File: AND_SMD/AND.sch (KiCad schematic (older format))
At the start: 8 parts, among them J1 Conn_01x08_Male, J2 Conn_01x08_Male, J3 Conn_01x08_Male, J4 Conn_01x04_Male, U1 74LS573, U2 74LS08, U3 74LS08

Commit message: Polishing AND SMD cmd
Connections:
- net at J1.8 (Pin_8): now also U2.2; no longer U2.1
- net at J2.8 (Pin_8): now also U2.1; no longer U2.2
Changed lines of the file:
@@
 U 1 1 5F5151F7
 P 3550 4400
-F 0 "U2" H 3500 4600 50  0000 C CNN
-F 1 "74LS08" H 3750 4600 50  0000 C CNN
+F 0 "U2" H 3475 4200 50  0000 C CNN
+F 1 "74LS08" H 3750 4200 50  0000 C CNN
 F 2 "Package_SO:SO-14_3.9x8.65mm_P1.27mm" H 3550 4400 50  0001 C CNN
 F 3 "http://www.ti.com/lit/gpn/sn74LS08" H 3550 4400 50  0001 C CNN
 	1    3550 4400
-	1    0    0    -1
+	1    0    0    1
 $EndComp
 $Comp

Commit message: AND SMD PCB is ready
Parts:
- added D1: LED, LED_SMD:LED_0805_2012Metric_Pad1.15x1.40mm_HandSolder, symbol Device:LED
- added R1: 1k, Resistor_SMD:R_0805_2012Metric_Pad1.20x1.40mm_HandSolder, symbol Device:R
- J1, J2, J3: footprint Connector_PinHeader_2.54mm:PinHeader_1x08_P2.54mm_Horizontal -> Connector_PinHeader_2.54mm:PinHeader_1x08_P2.54mm_Vertical
- J4: footprint Connector_PinHeader_2.54mm:PinHeader_1x04_P2.54mm_Horizontal -> Connector_PinHeader_2.54mm:PinHeader_1x04_P2.54mm_Vertical
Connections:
- net VCC: now also D1.1 (K)
- net A7: now reaches J1.1 (Pin_1), U3.9
- net A0: now reaches J1.8 (Pin_8), U2.2
- net B7: now reaches J2.1 (Pin_1), U3.10
- net B0: now reaches J2.8 (Pin_8), U2.1
- net OUT7: now reaches J3.1 (Pin_1), U1.19 (Q0)
- net OUT0: now reaches J3.8 (Pin_8), U1.12 (Q7)
- net ~OE: now reaches J4.1 (Pin_1), U1.1 (OE)
- net ~OE: now also R1.2
- net Latch: now reaches J4.4 (Pin_4), U1.11 (Load)
- new net: D1.2 (A), R1.1
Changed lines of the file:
@@
 F 0 "J1" H 1858 3581 50  0000 C CNN
 F 1 "Conn_01x08_Male" H 1858 3490 50  0000 C CNN
-F 2 "Connector_PinHeader_2.54mm:PinHeader_1x08_P2.54mm_Horizontal" H 1750 3100 50  0001 C CNN
+F 2 "Connector_PinHeader_2.54mm:PinHeader_1x08_P2.54mm_Vertical" H 1750 3100 50  0001 C CNN
 F 3 "~" H 1750 3100 50  0001 C CNN
 	1    1750 3100
@@
 F 0 "J2" H 1858 4581 50  0000 C CNN
 F 1 "Conn_01x08_Male" H 1858 4490 50  0000 C CNN
-F 2 "Connector_PinHeader_2.54mm:PinHeader_1x08_P2.54mm_Horizontal" H 1750 4100 50  0001 C CNN
+F 2 "Connector_PinHeader_2.54mm:PinHeader_1x08_P2.54mm_Vertical" H 1750 4100 50  0001 C CNN
 F 3 "~" H 1750 4100 50  0001 C CNN
 	1    1750 4100
@@
 F 0 "J3" H 7308 3831 50  0000 C CNN
 F 1 "Conn_01x08_Male" H 7300 2775 50  0000 C CNN
-F 2 "Connector_PinHeader_2.54mm:PinHeader_1x08_P2.54mm_Horizontal" H 7200 3350 50  0001 C CNN
+F 2 "Connector_PinHeader_2.54mm:PinHeader_1x08_P2.54mm_Vertical" H 7200 3350 50  0001 C CNN
 F 3 "~" H 7200 3350 50  0001 C CNN
 	1    7200 3350
@@
 F 0 "J4" H 1825 4775 50  0000 C CNN
 F 1 "Conn_01x04_Male" H 1625 5375 50  0000 C CNN
-F 2 "Connector_PinHeader_2.54mm:PinHeader_1x04_P2.54mm_Horizontal" H 1750 5150 50  0001 C CNN
+F 2 "Connector_PinHeader_2.54mm:PinHeader_1x04_P2.54mm_Vertical" H 1750 5150 50  0001 C CNN
 F 3 "~" H 1750 5150 50  0001 C CNN
 	1    1750 5150
@@
 	2025 5250 2025 5675
 Wire Wire Line
-	2025 5675 5750 5675
+	2025 5675 3725 5675
 Wire Wire Line
 	5750 5675 5750 4050
@@
 	1    0    0    -1
 $EndComp
+$Comp
+L Device:LED D1
+U 1 1 63459271
+P 3725 5225
+F 0 "D1" V 3672 5305 50  0000 L CNN
+F 1 "LED" V 3763 5305 50  0000 L CNN
+F 2 "LED_SMD:LED_0805_2012Metric_Pad1.15x1.40mm_HandSolder" H 3725 5225 50  0001 C CNN
+F 3 "~" H 3725 5225 50  0001 C CNN
+	1    3725 5225
+	0    1    1    0
+$EndComp
+$Comp
+L Device:R R1
+U 1 1 63459C8B
+P 3725 5525
+F 0 "R1" H 3795 5571 50  0000 L CNN
+F 1 "1k" V 3725 5475 50  0000 L CNN
+F 2 "Resistor_SMD:R_0805_2012Metric_Pad1.20x1.40mm_HandSolder" V 3655 5525 50  0001 C CNN
+F 3 "~" H 3725 5525 50  0001 C CNN
+	1    3725 5525
+	1    0    0    -1
+$EndComp
+Connection ~ 3725 5675
+Wire Wire Line
+	3725 5675 5750 5675
+$Comp
+L power:VCC #PWR03
+U 1 1 6345A840
+P 3725 5075
+F 0 "#PWR03" H 3725 4925 50  0001 C CNN
+F 1 "VCC" H 3742 5248 50  0000 C CNN
+F 2 "" H 3725 5075 50  0001 C CNN
+F 3 "" H 3725 5075 50  0001 C CNN
+	1    3725 5075
+	1    0    0    -1
+$EndComp
+Text Label 2000 3500 0    50   ~ 0
+A0
+Text Label 2000 2800 0    50   ~ 0
+A7
+Text Label 2025 4500 0    50   ~ 0
+B0
+Text Label 1975 3800 0    50   ~ 0
+B7
+Text Label 6800 3750 0    50   ~ 0
+OUT0
+Text Label 6800 3050 0    50   ~ 0
+OUT7
+Text Label 1975 5250 0    50   ~ 0
+~OE
+Text Label 2025 4625 0    50   ~ 0
+Latch
 $EndSCHEMATC

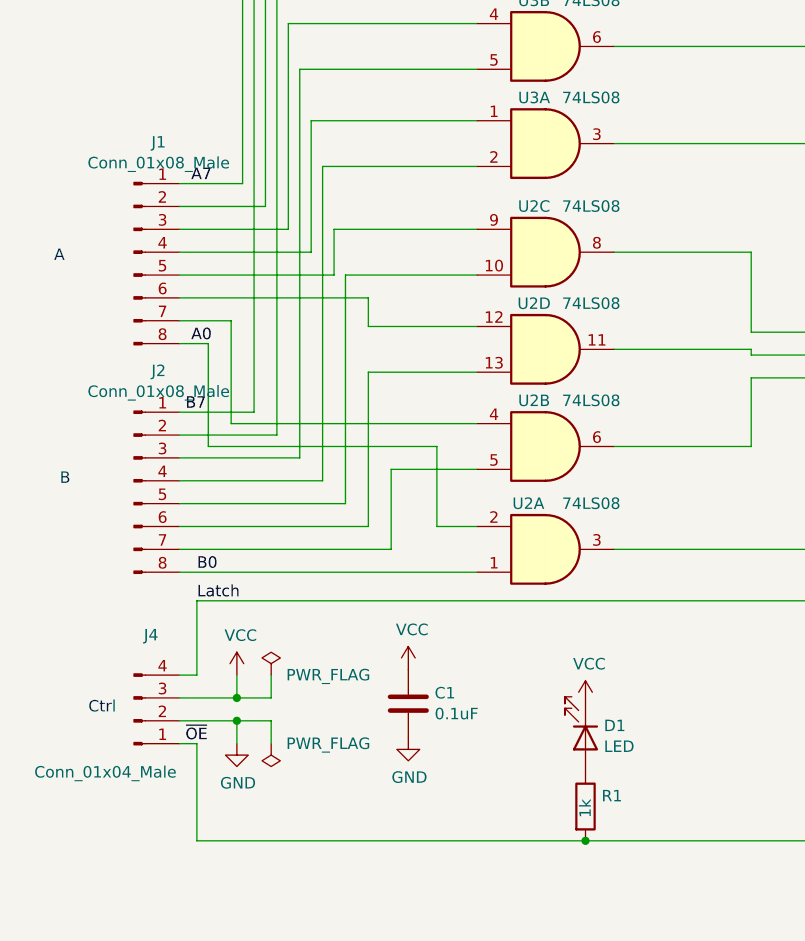
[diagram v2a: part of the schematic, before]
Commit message: Swap A & B busses.
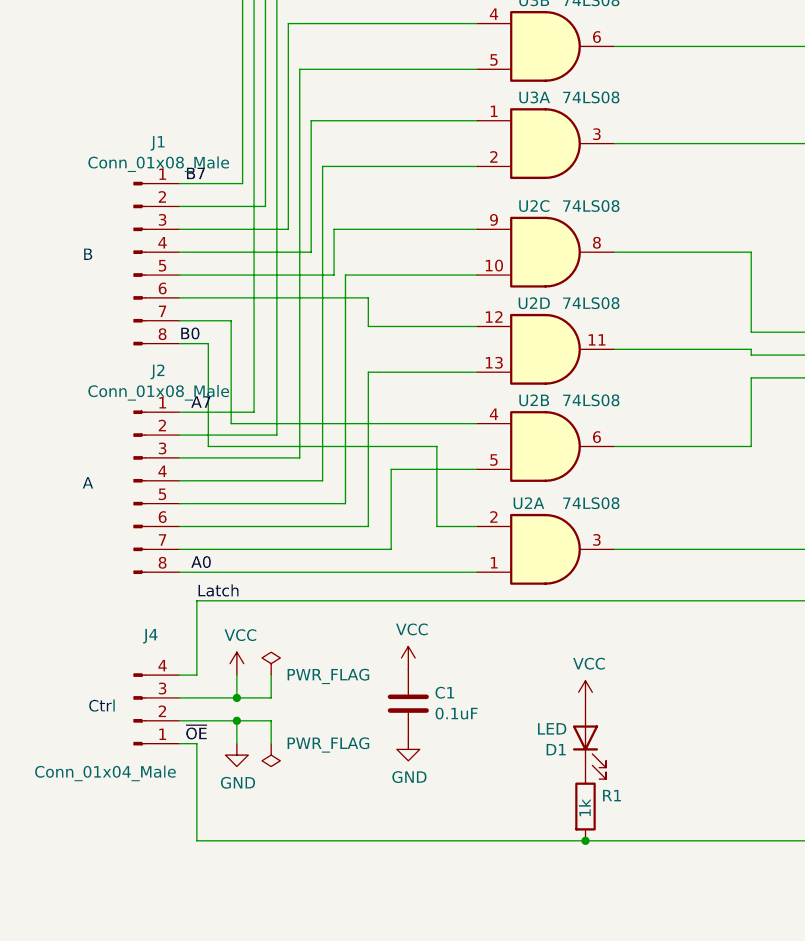
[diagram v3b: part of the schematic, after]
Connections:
- net A0: now also J2.8 (Pin_8), U2.1; no longer J1.8 (Pin_8), U2.2
- net A7: now also J2.1 (Pin_1), U3.10; no longer J1.1 (Pin_1), U3.9
- net B0: now also J1.8 (Pin_8), U2.2; no longer J2.8 (Pin_8), U2.1
- net B7: now also J1.1 (Pin_1), U3.9; no longer J2.1 (Pin_1), U3.10
- net VCC: now also D1.2 (A); no longer D1.1 (K)
- net at R1.1: now also D1.1 (K); no longer D1.2 (A)
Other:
- moved on the sheet: D1
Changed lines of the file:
@@
 	1    0    0    1
 $EndComp
-Text Notes 1400 3150 0    50   ~ 0
+Text Notes 1525 4150 0    50   ~ 0
 A
-Text Notes 1425 4125 0    50   ~ 0
+Text Notes 1525 3150 0    50   ~ 0
 B
 Text Notes 7375 3425 0    50   ~ 0
@@
 F 3 "~" H 3725 5225 50  0001 C CNN
 	1    3725 5225
-	0    1    1    0
+	0    -1   -1   0
 $EndComp
 $Comp
@@
 	1    0    0    -1
 $EndComp
-Text Label 2000 3500 0    50   ~ 0
+Text Label 2000 4500 0    50   ~ 0
 A0
-Text Label 2000 2800 0    50   ~ 0
+Text Label 2000 3800 0    50   ~ 0
 A7
-Text Label 2025 4500 0    50   ~ 0
+Text Label 1950 3500 0    50   ~ 0
 B0
-Text Label 1975 3800 0    50   ~ 0
+Text Label 1975 2800 0    50   ~ 0
 B7
 Text Label 6800 3750 0    50   ~ 0
